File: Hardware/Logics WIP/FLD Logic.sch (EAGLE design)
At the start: 82 parts

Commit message: 
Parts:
- added H1, H2, H3, H4: MOUNT-HOLE3.3, holes:MOUNT-HOLE3.3
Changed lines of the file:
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@@
 <part name="V42" library="supply0" deviceset="+5V" device=""/>
 <part name="OUT" library="pinhead" deviceset="PINHD-1X3" device=""/>
+<part name="H1" library="holes" deviceset="MOUNT-HOLE" device="3.3"/>
+<part name="H2" library="holes" deviceset="MOUNT-HOLE" device="3.3"/>
+<part name="H3" library="holes" deviceset="MOUNT-HOLE" device="3.3"/>
+<part name="H4" library="holes" deviceset="MOUNT-HOLE" device="3.3"/>
 </parts>
 <sheets>
@@
 <instance part="V42" gate="1" x="312.42" y="226.06"/>
 <instance part="OUT" gate="A" x="325.12" y="213.36"/>
+<instance part="H1" gate="G$1" x="-7.62" y="-81.28"/>
+<instance part="H2" gate="G$1" x="0" y="170.18"/>
+<instance part="H3" gate="G$1" x="391.16" y="160.02"/>
+<instance part="H4" gate="G$1" x="381" y="-76.2"/>
 </instances>
 <busses>

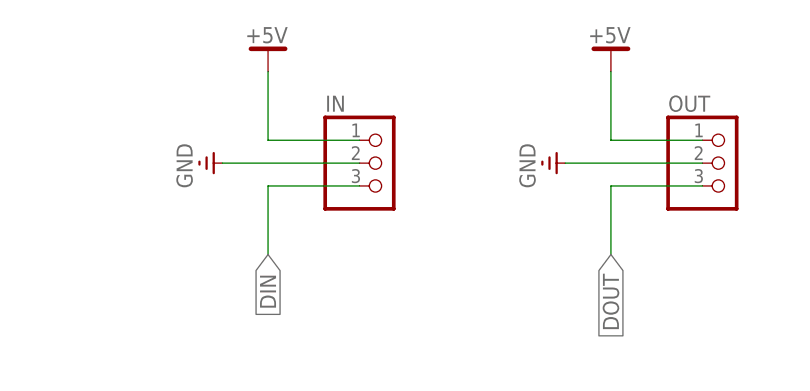
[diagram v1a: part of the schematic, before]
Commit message: 
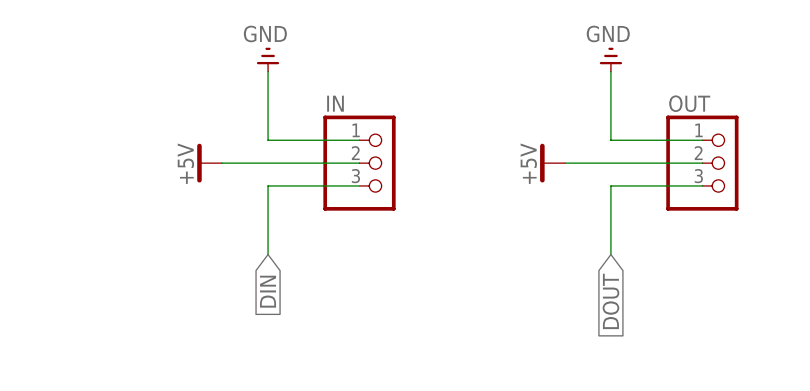
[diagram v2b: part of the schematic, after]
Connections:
- net +5V: now also IN.2, OUT.2; no longer IN.1, OUT.1
- net GND: now also IN.1, OUT.1; no longer IN.2, OUT.2
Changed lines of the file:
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@@
 </classes>
 <parts>
-<part name="GND3" library="supply0" deviceset="GND" device=""/>
-<part name="V9" library="supply0" deviceset="+5V" device=""/>
 <part name="LED1" library="adafruit" deviceset="WS2812" device=""/>
 <part name="LED2" library="adafruit" deviceset="WS2812" device=""/>
@@
 <part name="GND80" library="supply0" deviceset="GND" device=""/>
 <part name="GND81" library="supply0" deviceset="GND" device=""/>
-<part name="GND82" library="supply0" deviceset="GND" device=""/>
-<part name="V42" library="supply0" deviceset="+5V" device=""/>
 <part name="OUT" library="pinhead" deviceset="PINHD-1X3" device=""/>
 <part name="H1" library="holes" deviceset="MOUNT-HOLE" device="3.3"/>
@@
 <part name="H3" library="holes" deviceset="MOUNT-HOLE" device="3.3"/>
 <part name="H4" library="holes" deviceset="MOUNT-HOLE" device="3.3"/>
+<part name="V9" library="supply0" deviceset="+5V" device=""/>
+<part name="GND3" library="supply0" deviceset="GND" device=""/>
+<part name="V42" library="supply0" deviceset="+5V" device=""/>
+<part name="GND82" library="supply0" deviceset="GND" device=""/>
 </parts>
 <sheets>
@@
 </plain>
 <instances>
-<instance part="GND3" gate="1" x="266.7" y="213.36" rot="R270"/>
-<instance part="V9" gate="1" x="274.32" y="226.06"/>
 <instance part="LED1" gate="G$1" x="66.04" y="154.94"/>
 <instance part="LED2" gate="G$1" x="99.06" y="154.94"/>
@@
 <instance part="GND80" gate="1" x="264.16" y="-73.66"/>
 <instance part="GND81" gate="1" x="297.18" y="-73.66"/>
-<instance part="GND82" gate="1" x="304.8" y="213.36" rot="R270"/>
-<instance part="V42" gate="1" x="312.42" y="226.06"/>
 <instance part="OUT" gate="A" x="325.12" y="213.36"/>
 <instance part="H1" gate="G$1" x="-7.62" y="-81.28"/>
@@
 <instance part="H3" gate="G$1" x="391.16" y="160.02"/>
 <instance part="H4" gate="G$1" x="381" y="-76.2"/>
+<instance part="V9" gate="1" x="266.7" y="213.36" rot="R90"/>
+<instance part="GND3" gate="1" x="274.32" y="226.06" rot="R180"/>
+<instance part="V42" gate="1" x="304.8" y="213.36" rot="R90"/>
+<instance part="GND82" gate="1" x="312.42" y="226.06" rot="R180"/>
 </instances>
 <busses>
@@
 </segment>
 <segment>
-<pinref part="IN" gate="A" pin="2"/>
-<wire x1="284.48" y1="213.36" x2="269.24" y2="213.36" width="0.1524" layer="91"/>
-<pinref part="GND3" gate="1" pin="GND"/>
-</segment>
-<segment>
 <pinref part="LED1" gate="G$1" pin="GND"/>
 <pinref part="GND7" gate="1" pin="GND"/>
@@
 </segment>
 <segment>
-<pinref part="OUT" gate="A" pin="2"/>
-<wire x1="322.58" y1="213.36" x2="307.34" y2="213.36" width="0.1524" layer="91"/>
+<pinref part="IN" gate="A" pin="1"/>
+<wire x1="284.48" y1="215.9" x2="274.32" y2="215.9" width="0.1524" layer="91"/>
+<wire x1="274.32" y1="215.9" x2="274.32" y2="223.52" width="0.1524" layer="91"/>
+<pinref part="GND3" gate="1" pin="GND"/>
+</segment>
+<segment>
+<pinref part="OUT" gate="A" pin="1"/>
+<wire x1="322.58" y1="215.9" x2="312.42" y2="215.9" width="0.1524" layer="91"/>
+<wire x1="312.42" y1="215.9" x2="312.42" y2="223.52" width="0.1524" layer="91"/>
 <pinref part="GND82" gate="1" pin="GND"/>
 </segment>
@@
 </segment>
 <segment>
-<pinref part="IN" gate="A" pin="1"/>
-<wire x1="284.48" y1="215.9" x2="274.32" y2="215.9" width="0.1524" layer="91"/>
-<wire x1="274.32" y1="215.9" x2="274.32" y2="223.52" width="0.1524" layer="91"/>
-<pinref part="V9" gate="1" pin="+5V"/>
-</segment>
-<segment>
 <pinref part="V1" gate="1" pin="+5V"/>
 <wire x1="157.48" y1="180.34" x2="157.48" y2="177.8" width="0.1524" layer="91"/>
@@
 </segment>
 <segment>
-<pinref part="OUT" gate="A" pin="1"/>
-<wire x1="322.58" y1="215.9" x2="312.42" y2="215.9" width="0.1524" layer="91"/>
-<wire x1="312.42" y1="215.9" x2="312.42" y2="223.52" width="0.1524" layer="91"/>
+<pinref part="IN" gate="A" pin="2"/>
+<wire x1="284.48" y1="213.36" x2="269.24" y2="213.36" width="0.1524" layer="91"/>
+<pinref part="V9" gate="1" pin="+5V"/>
+</segment>
+<segment>
+<pinref part="OUT" gate="A" pin="2"/>
+<wire x1="322.58" y1="213.36" x2="307.34" y2="213.36" width="0.1524" layer="91"/>
 <pinref part="V42" gate="1" pin="+5V"/>
 </segment>
